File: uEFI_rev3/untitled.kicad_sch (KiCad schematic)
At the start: 27 parts, among them U36 MAX9926UAEE+

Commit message: uEFI rev 3.1.0
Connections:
- net +5VA renamed +3V3
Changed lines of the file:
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@@
+    (pin "1")
+  )
+  (symbol (lib_id "power:+3V3") (at 173.99 74.93 0) (unit 1)
+    (in_bom yes) (on_board yes) (fields_autoplaced)
+    (property "Reference" "#PWR0162" (id 0) (at 173.99 78.74 0)
+      (effects (font (size 1.27 1.27)) hide)
+    )
+    (property "Value" "" (id 1) (at 173.99 69.85 0))
+    (property "Footprint" "" (id 2) (at 173.99 74.93 0)
+      (effects (font (size 1.27 1.27)) hide)
+    )
+    (property "Datasheet" "" (id 3) (at 173.99 74.93 0)
+      (effects (font (size 1.27 1.27)) hide)
+    )
     (pin "1")
   )
@@
     (pin "2")
   )
-  (symbol (lib_id "power:+5VA") (at 173.99 74.93 0) (unit 1)
-    (in_bom yes) (on_board yes)
-    (property "Reference" "#PWR0178" (id 0) (at 173.99 78.74 0)
-      (effects (font (size 1.27 1.27)) hide)
-    )
-    (property "Value" "+5VA" (id 1) (at 174.3583 70.6056 0))
-    (property "Footprint" "" (id 2) (at 173.99 74.93 0)
-      (effects (font (size 1.27 1.27)) hide)
-    )
-    (property "Datasheet" "" (id 3) (at 173.99 74.93 0)
-      (effects (font (size 1.27 1.27)) hide)
-    )
-    (pin "1")
-  )
   (symbol (lib_id "power:GND") (at 78.74 135.89 0) (unit 1)

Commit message: wip v3.1
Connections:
- net +3V3: no longer U36.14 (VCC)
- new net +5V: U36.14 (VCC)
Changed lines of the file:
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@@
   (junction (at 116.205 78.74) (diameter 1.016) (color 0 0 0 0)
   )
-  (junction (at 180.34 77.47) (diameter 1.016) (color 0 0 0 0)
-  )
   (junction (at 191.77 85.09) (diameter 1.016) (color 0 0 0 0)
   )
@@
   (junction (at 132.08 85.09) (diameter 1.016) (color 0 0 0 0)
   )
+  (junction (at 191.77 77.47) (diameter 0) (color 0 0 0 0)
+  )
   (junction (at 132.08 107.95) (diameter 1.016) (color 0 0 0 0)
   )
@@
   )
   (junction (at 124.46 125.095) (diameter 0.9144) (color 0 0 0 0)
-  )
-  (junction (at 173.99 77.47) (diameter 1.016) (color 0 0 0 0)
   )
   (junction (at 198.12 82.55) (diameter 0.9144) (color 0 0 0 0)
@@
     (stroke (width 0) (type solid) (color 0 0 0 0))
   )
+  (wire (pts (xy 191.77 76.2) (xy 191.77 77.47))
+    (stroke (width 0) (type default) (color 0 0 0 0))
+  )
   (wire (pts (xy 135.89 95.25) (xy 125.73 95.25))
     (stroke (width 0) (type solid) (color 0 0 0 0))
@@
   )
   (wire (pts (xy 106.045 113.03) (xy 106.045 115.57))
-    (stroke (width 0) (type solid) (color 0 0 0 0))
-  )
-  (wire (pts (xy 173.99 77.47) (xy 180.34 77.47))
     (stroke (width 0) (type solid) (color 0 0 0 0))
   )
@@
     (pin "2")
   )
+  (symbol (lib_id "power:+5V") (at 173.99 74.93 0) (unit 1)
+    (in_bom yes) (on_board yes)
+    (property "Reference" "#PWR0163" (id 0) (at 173.99 78.74 0)
+      (effects (font (size 1.27 1.27)) hide)
+    )
+    (property "Value" "+5V" (id 1) (at 174.371 70.5358 0))
+    (property "Footprint" "" (id 2) (at 173.99 74.93 0)
+      (effects (font (size 1.27 1.27)) hide)
+    )
+    (property "Datasheet" "" (id 3) (at 173.99 74.93 0)
+      (effects (font (size 1.27 1.27)) hide)
+    )
+    (pin "1")
+  )
   (symbol (lib_id "power:GND") (at 132.08 124.46 0) (unit 1)
     (in_bom yes) (on_board yes)
@@
     (pin "1")
   )
-  (symbol (lib_id "power:+3V3") (at 173.99 74.93 0) (unit 1)
+  (symbol (lib_id "power:+3V3") (at 191.77 76.2 0) (unit 1)
     (in_bom yes) (on_board yes) (fields_autoplaced)
-    (property "Reference" "#PWR0162" (id 0) (at 173.99 78.74 0)
-      (effects (font (size 1.27 1.27)) hide)
-    )
-    (property "Value" "" (id 1) (at 173.99 69.85 0))
-    (property "Footprint" "" (id 2) (at 173.99 74.93 0)
-      (effects (font (size 1.27 1.27)) hide)
-    )
-    (property "Datasheet" "" (id 3) (at 173.99 74.93 0)
-      (effects (font (size 1.27 1.27)) hide)
-    )
+    (property "Reference" "#PWR0162" (id 0) (at 191.77 80.01 0)
+      (effects (font (size 1.27 1.27)) hide)
+    )
+    (property "Value" "+3V3" (id 1) (at 191.77 71.12 0))
+    (property "Footprint" "" (id 2) (at 191.77 76.2 0)
+      (effects (font (size 1.27 1.27)) hide)
+    )
+    (property "Datasheet" "" (id 3) (at 191.77 76.2 0)
+      (effects (font (size 1.27 1.27)) hide)
+    )

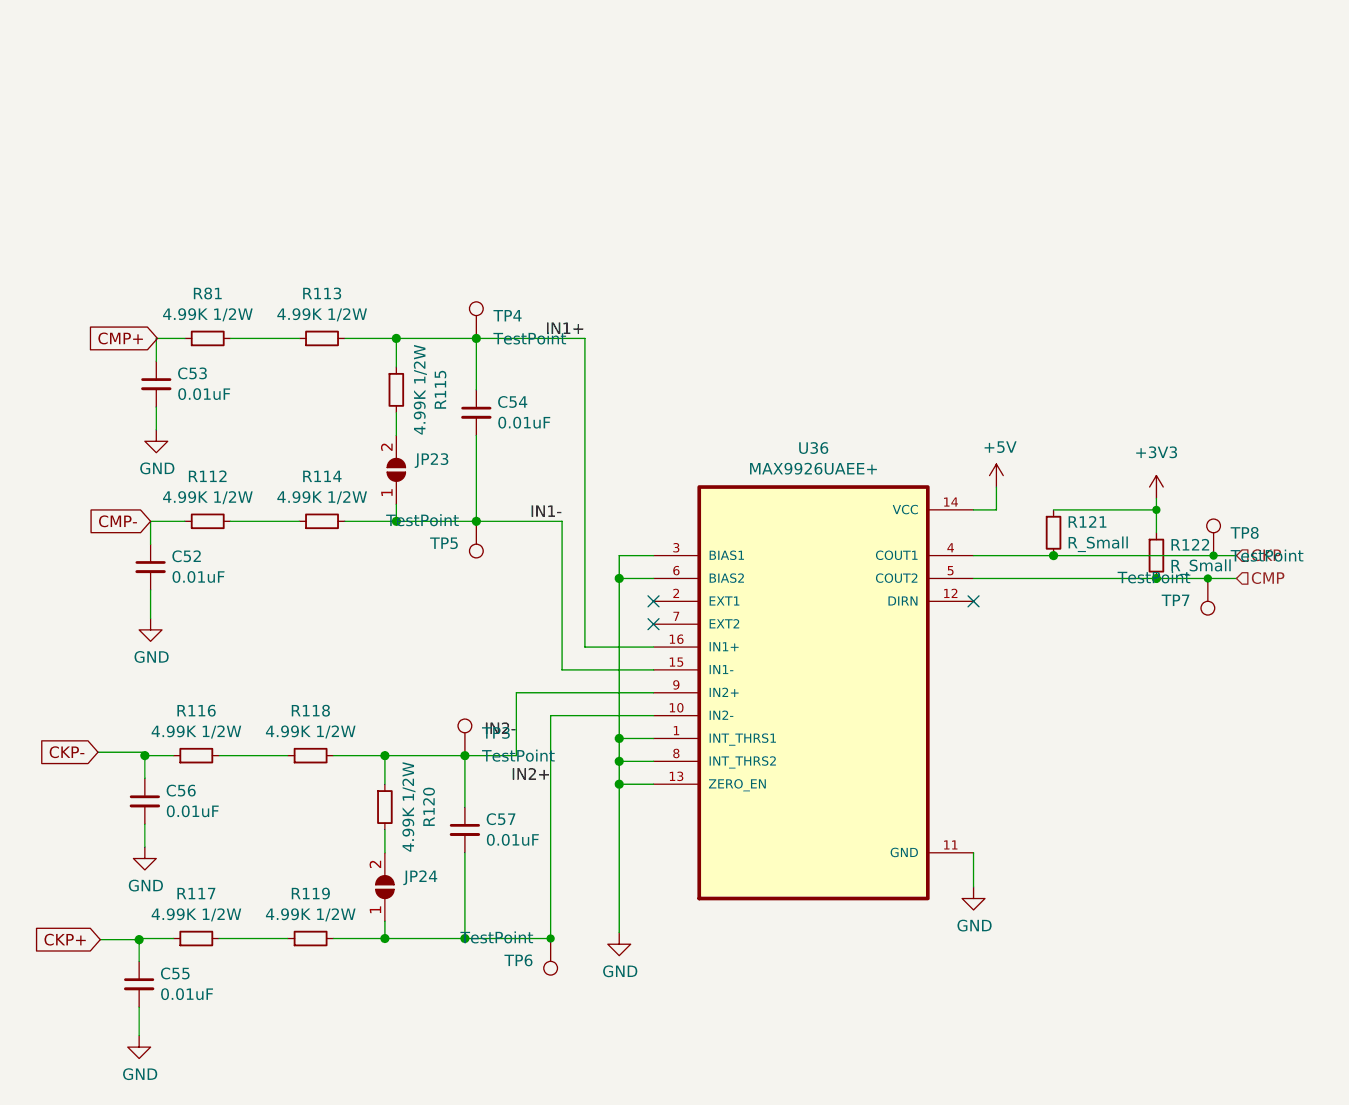
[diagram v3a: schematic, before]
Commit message: add ckp sensor setup
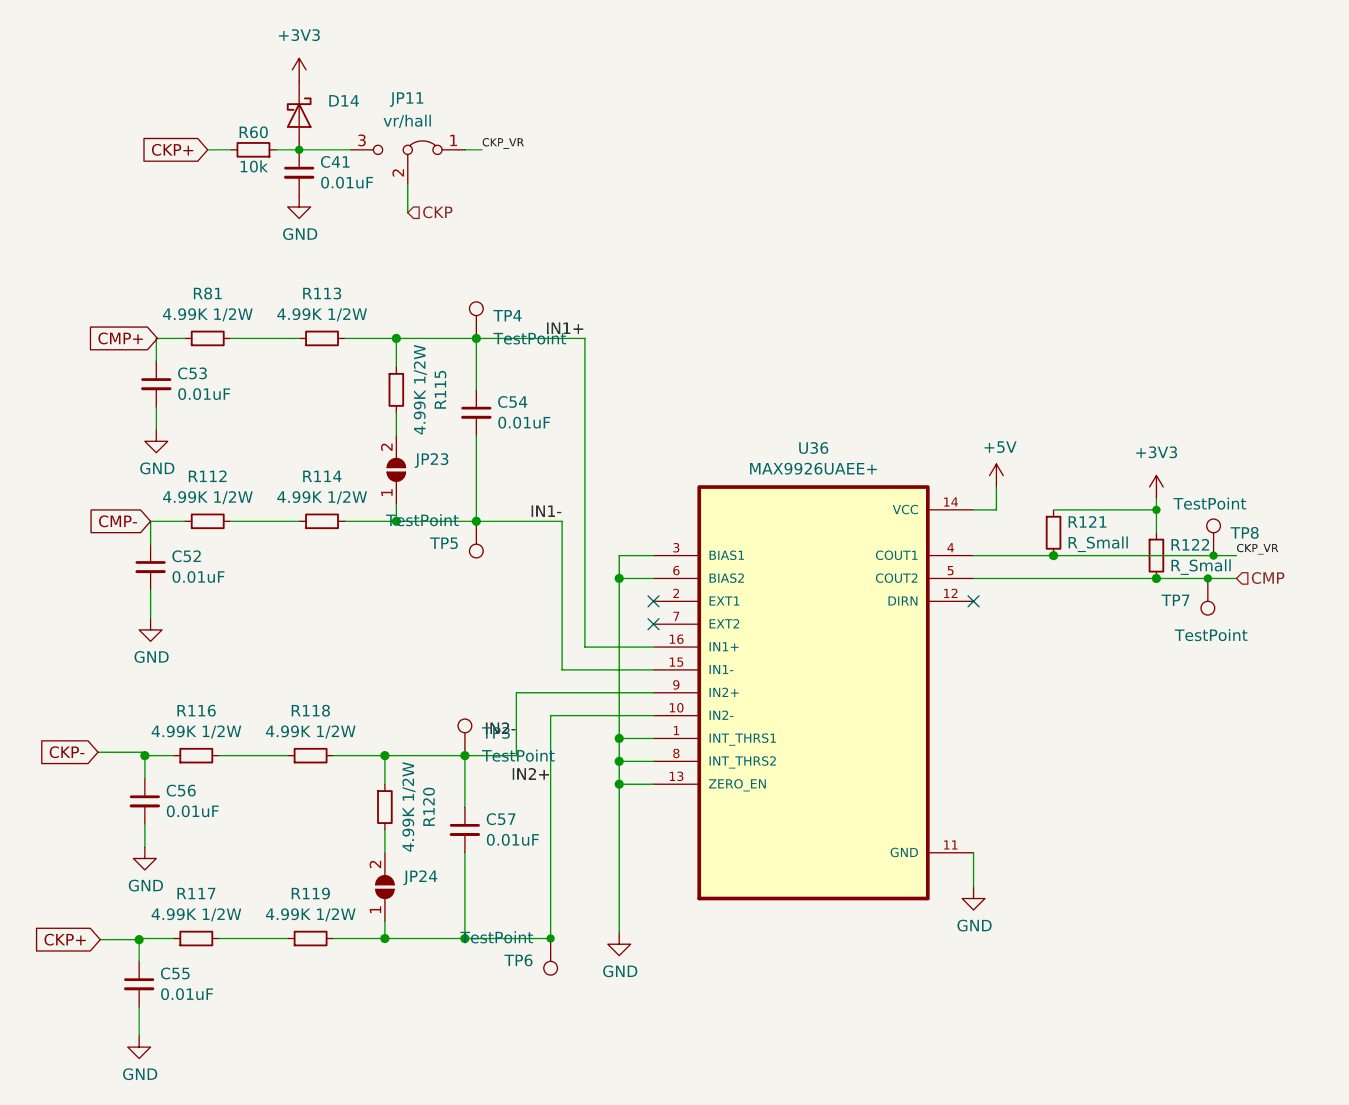
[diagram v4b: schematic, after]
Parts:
- added C41: 0.01uF, Capacitor_SMD:C_0805_2012Metric, symbol Device:C_Small
- added D14: K26, Diode_SMD:D_SOD-123F, symbol Diode:PMEG2020EH
- added JP11: vr/hall, Jumper:SolderJumper-3_P1.3mm_Bridged2Bar12_Pad1.0x1.5mm_NumberLabels, symbol Jumper:Jumper_3_Bridged12
- added R60: 10k, Resistor_SMD:R_0603_1608Metric, symbol Device:R_Small
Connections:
- net +3V3: now also D14.1 (K)
- net CKP: now also JP11.2 (C); no longer R121.2, TP8.1, U36.4 (COUT1)
- net CKP+: now also R60.2
- net GND: now also C41.2
- new net: C41.1, D14.2 (A), JP11.3 (B), R60.1
- new net CKP_VR: JP11.1 (A), R121.2, TP8.1, U36.4 (COUT1)
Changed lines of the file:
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@@
   (junction (at 132.08 107.95) (diameter 1.016) (color 0 0 0 0)
+  )
+  (junction (at 96.52 37.465) (diameter 0) (color 0 0 0 0)
   )
   (junction (at 79.375 104.775) (diameter 1.016) (color 0 0 0 0)
@@
     (stroke (width 0) (type solid) (color 0 0 0 0))
   )
+  (wire (pts (xy 114.935 37.465) (xy 116.84 37.465))
+    (stroke (width 0) (type default) (color 0 0 0 0))
+  )
   (wire (pts (xy 135.89 82.55) (xy 132.08 82.55))
     (stroke (width 0) (type solid) (color 0 0 0 0))
@@
     (stroke (width 0) (type solid) (color 0 0 0 0))
   )
+  (wire (pts (xy 86.36 37.465) (xy 88.9 37.465))
+    (stroke (width 0) (type default) (color 0 0 0 0))
+  )
   (wire (pts (xy 120.65 104.775) (xy 114.935 104.775))
     (stroke (width 0) (type solid) (color 0 0 0 0))
@@
     (stroke (width 0) (type solid) (color 0 0 0 0))
   )
+  (wire (pts (xy 93.98 37.465) (xy 96.52 37.465))
+    (stroke (width 0) (type default) (color 0 0 0 0))
+  )
+  (wire (pts (xy 108.585 41.275) (xy 108.585 44.45))
+    (stroke (width 0) (type default) (color 0 0 0 0))
+  )
   (wire (pts (xy 173.99 77.47) (xy 171.45 77.47))
     (stroke (width 0) (type solid) (color 0 0 0 0))
@@
   (wire (pts (xy 106.045 113.03) (xy 106.045 115.57))
     (stroke (width 0) (type solid) (color 0 0 0 0))
+  )
+  (wire (pts (xy 96.52 37.465) (xy 102.235 37.465))
+    (stroke (width 0) (type default) (color 0 0 0 0))
   )
   (label "IN1+" (at 128.27 58.42 180)
@@
     (effects (font (size 1.27 1.27)) (justify right bottom))
   )
+  (label "CKP_VR" (at 116.84 37.465 0)
+    (effects (font (size 0.889 0.889)) (justify left bottom))
+  )
   (label "IN1-" (at 125.73 78.74 180)
     (effects (font (size 1.27 1.27)) (justify right bottom))
+  )
+  (label "CKP_VR" (at 200.66 82.55 0)
+    (effects (font (size 0.889 0.889)) (justify left bottom))
   )
   (label "IN2+" (at 124.46 107.95 180)
@@
     )
   )
+  (global_label "CKP+" (shape input) (at 86.36 37.465 180)
+    (effects (font (size 1.27 1.27)) (justify right))
+    (property "Intersheet References" "${INTERSHEET_REFS}" (id 0) (at 78.5645 37.3856 0)
+      (effects (font (size 1.27 1.27)) (justify right) hide)
+    )
+  )
   (global_label "CKP-" (shape input) (at 74.168 104.394 180)
     (effects (font (size 1.27 1.27)) (justify right))
@@
     )
   )
+  (hierarchical_label "CKP" (shape input) (at 108.585 44.45 0)
+    (effects (font (size 1.27 1.27)) (justify left))
+  )
   (hierarchical_label "CMP" (shape input) (at 200.66 85.09 0)
-    (effects (font (size 1.27 1.27)) (justify left))
-  )
-  (hierarchical_label "CKP" (shape input) (at 200.66 82.55 0)
     (effects (font (size 1.27 1.27)) (justify left))
   )
@@
     (pin "2")
   )
+  (symbol (lib_id "Device:R_Small") (at 91.44 37.465 270) (mirror x) (unit 1)
+    (in_bom yes) (on_board yes)
+    (property "Reference" "R60" (id 0) (at 91.44 35.56 90))
+    (property "Value" "10k" (id 1) (at 91.44 39.37 90))
+    (property "Footprint" "Resistor_SMD:R_0603_1608Metric" (id 2) (at 91.44 37.465 0)
+      (effects (font (size 1.27 1.27)) hide)
+    )
+    (property "Datasheet" "~" (id 3) (at 91.44 37.465 0)
+      (effects (font (size 1.27 1.27)) hide)
+    )
+    (pin "1")
+    (pin "2")
+  )
   (symbol (lib_id "power:GND") (at 80.01 89.535 0) (unit 1)
     (in_bom yes) (on_board yes)
@@
     (pin "2")
   )
+  (symbol (lib_id "Device:C_Small") (at 96.52 40.005 0) (unit 1)
+    (in_bom yes) (on_board yes)
+    (property "Reference" "C41" (id 0) (at 98.8442 38.8556 0)
+      (effects (font (size 1.27 1.27)) (justify left))
+    )
+    (property "Value" "0.01uF" (id 1) (at 98.8442 41.1543 0)
+      (effects (font (size 1.27 1.27)) (justify left))
+    )
+    (property "Footprint" "Capacitor_SMD:C_0805_2012Metric" (id 2) (at 96.52 40.005 0)
+      (effects (font (size 1.27 1.27)) hide)
+    )
+    (property "Datasheet" "~" (id 3) (at 96.52 40.005 0)
+      (effects (font (size 1.27 1.27)) hide)
+    )
+    (property "LCSC" "C100042" (id 4) (at 96.52 40.005 0)
+      (effects (font (size 1.27 1.27)) hide)
+    )
+    (pin "1")
+    (pin "2")
+  )
   (symbol (lib_id "Connector:TestPoint") (at 116.205 78.74 180) (unit 1)
     (in_bom yes) (on_board yes)
@@
       (effects (font (size 1.27 1.27)) (justify left))
     )
-    (property "Value" "TestPoint" (id 1) (at 195.58 85.0266 0)
+    (property "Value" "TestPoint" (id 1) (at 201.93 91.44 0)
       (effects (font (size 1.27 1.27)) (justify left))
     )
@@
     (pin "2")
   )
+  (symbol (lib_id "Diode:PMEG2020EH") (at 96.52 33.655 270) (unit 1)
+    (in_bom yes) (on_board yes) (fields_autoplaced)
+    (property "Reference" "D14" (id 0) (at 99.695 32.0674 90)
+      (effects (font (size 1.27 1.27)) (justify left))
+    )
+    (property "Value" "K26" (id 1) (at 99.695 34.6074 90)
+      (effects (font (size 1.27 1.27)) (justify left) hide)
+    )
+    (property "Footprint" "Diode_SMD:D_SOD-123F" (id 2) (at 92.075 33.655 0)
+      (effects (font (size 1.27 1.27)) hide)
+    )
+    (property "Datasheet" "https://datasheet.lcsc.com/lcsc/2111221830_GOODWORK-K26_C2922179.pdf" (id 3) (at 96.52 33.655 0)
+      (effects (font (size 1.27 1.27)) hide)
+    )
+    (property "LCSC" "C2922179" (id 4) (at 96.52 33.655 90)
+      (effects (font (size 0.889 0.889)) hide)
+    )
+    (pin "1")
+    (pin "2")
+  )
+  (symbol (lib_id "Jumper:Jumper_3_Bridged12") (at 108.585 37.465 0) (mirror y) (unit 1)
+    (in_bom yes) (on_board yes) (fields_autoplaced)
+    (property "Reference" "JP11" (id 0) (at 108.585 31.75 0))
+    (property "Value" "vr/hall" (id 1) (at 108.585 34.29 0))
+    (property "Footprint" "Jumper:SolderJumper-3_P1.3mm_Bridged2Bar12_Pad1.0x1.5mm_NumberLabels" (id 2) (at 108.585 37.465 0)
+      (effects (font (size 1.27 1.27)) hide)
+    )
+    (property "Datasheet" "~" (id 3) (at 108.585 37.465 0)
+      (effects (font (size 1.27 1.27)) hide)
+    )
+    (pin "1")
+    (pin "2")
+    (pin "3")
+  )
   (symbol (lib_id "Device:R_Small") (at 191.77 82.55 0) (unit 1)
     (in_bom yes) (on_board yes)
@@
     (pin "1")
     (pin "2")
+  )
+  (symbol (lib_id "power:+3V3") (at 96.52 29.845 0) (unit 1)
+    (in_bom yes) (on_board yes) (fields_autoplaced)
+    (property "Reference" "#PWR055" (id 0) (at 96.52 33.655 0)
+      (effects (font (size 1.27 1.27)) hide)
+    )
+    (property "Value" "+3V3" (id 1) (at 96.52 24.765 0))
+    (property "Footprint" "" (id 2) (at 96.52 29.845 0)
+      (effects (font (size 1.27 1.27)) hide)
+    )
+    (property "Datasheet" "" (id 3) (at 96.52 29.845 0)
+      (effects (font (size 1.27 1.27)) hide)
+    )
+    (pin "1")
   )
   (symbol (lib_id "Connector:TestPoint") (at 124.46 125.095 180) (unit 1)
@@
     (pin "2")
   )
+  (symbol (lib_id "power:GND") (at 96.52 42.545 0) (unit 1)
+    (in_bom yes) (on_board yes)
+    (property "Reference" "#PWR058" (id 0) (at 96.52 48.895 0)
+      (effects (font (size 1.27 1.27)) hide)
+    )
+    (property "Value" "GND" (id 1) (at 96.6343 46.8694 0))
+    (property "Footprint" "" (id 2) (at 96.52 42.545 0)
+      (effects (font (size 1.27 1.27)) hide)
+    )
+    (property "Datasheet" "" (id 3) (at 96.52 42.545 0)
+      (effects (font (size 1.27 1.27)) hide)
+    )
+    (pin "1")
+  )
   (symbol (lib_id "Device:R_Small") (at 97.79 125.095 90) (unit 1)
     (in_bom yes) (on_board yes)
@@
       (effects (font (size 1.27 1.27)) (justify left))
     )
-    (property "Value" "TestPoint" (id 1) (at 200.025 82.6134 0)
-      (effects (font (size 1.27 1.27)) (justify left))
-    )
+    (property "Value" "TestPoint" (id 1) (at 193.675 76.835 0)
+      (effects (font (size 1.27 1.27)) (justify left))
+    )
